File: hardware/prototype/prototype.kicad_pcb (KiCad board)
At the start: 2 copper layers, 177.8 x 111.8 mm, 91 parts, among them J1 0734120114, J2 Conn_01x04, J4 Conn_01x04, J5 Conn_02x07_Odd_Even, J6 Battery-holder, J7 Conn_02x12_Odd_Even, J8 Jack-DC, Q1 DTC143Z, Q2 Si2323, U1 QUECTEL_L80, U2 TLV71333PDBV, U3 LM2596_MODULE, U4 DevkitC, U5 MIKROE_3G_CLICK

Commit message: Complete PCB layout
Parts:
- removed D10, D13, D14, D15, D16, D17, D18, D7, D8, D9: D_TVS, Diode_SMD:D_0402_1005Metric
- removed D11, D12: D_TVS, digikey-footprints:DO-214AC
- removed D19, D20: LED, LED_SMD:LED_0805_2012Metric_Pad0.97x1.50mm_HandSolder
- removed J8: Jack-DC, Connector_BarrelJack:BarrelJack_Horizontal
- removed TP1: Test_Point_Probe, TestPoint:TestPoint_Pad_D1.0mm
- added G***: LOGO, logo:LoRa_logo, F.Cu at (115.6, 124.5)
- added J3: Conn_01x04, lib_fp:PinHeader_1x04_P2.54mm_staggered_Vertical, F.Cu at (182.4, 110.2)
- C10, C16: value 220uF -> 0.1uF; footprint Capacitor_SMD:CP_Elec_6.3x5.8 -> Capacitor_SMD:C_0805_2012Metric_Pad1.15x1.50mm_HandSolder
- C12, C15: value 0.1uF -> 220uF; footprint Capacitor_SMD:C_0805_2012Metric_Pad1.15x1.50mm_HandSolder -> Capacitor_SMD:CP_Elec_6.3x5.8
- C2: value 0.1uF -> 10uF
- C3: value 10uF -> 1uF
- C4: value 1uF -> 0.1uF
- D1, D2: value LED -> D_TVS; footprint LED_SMD:LED_0805_2012Metric_Pad0.97x1.50mm_HandSolder -> digikey-footprints:DO-214AC
- D3, D4, D5, D6: value D_TVS -> LED; footprint Diode_SMD:D_0402_1005Metric -> LED_SMD:LED_0805_2012Metric_Pad0.97x1.50mm_HandSolder
- J1: value 0734120114 -> Jack-DC; footprint digikey-footprints:Molex_734120114_UMC_RF_CONN_Vertical -> Connector_BarrelJack:BarrelJack_Horizontal
- J2: value Conn_01x04 -> 0734120114; footprint lib_fp:PinHeader_1x04_P2.54mm_staggered_Vertical -> digikey-footprints:Molex_734120114_UMC_RF_CONN_Vertical
- JP17: value Jumper -> Jumper_NC_Dual; footprint lib_fp:PinHeader_1x02_P2.54mm_staggered_Vertical -> lib_fp:PinHeader_1x03_P2.54mm_staggered_Vertical
- JP19: value SolderJumper_2_Open -> Jumper; footprint Jumper:SolderJumper-2_P1.3mm_Open_RoundedPad1.0x1.5mm -> lib_fp:PinHeader_1x02_P2.54mm_staggered_Vertical
- JP21: value Jumper -> SolderJumper_2_Open; footprint lib_fp:PinHeader_1x02_P2.54mm_staggered_Vertical -> Jumper:SolderJumper-2_P1.3mm_Open_RoundedPad1.0x1.5mm
- Q1: value DTC143Z -> Si2323; footprint Package_TO_SOT_SMD:SC-59_Handsoldering -> Package_TO_SOT_SMD:SOT-23
- Q2: value Si2323 -> DTC143Z; footprint Package_TO_SOT_SMD:SOT-23 -> Package_TO_SOT_SMD:SC-59_Handsoldering
- R2: value 110R -> 10k
- R5: value 10k -> 4.7k
- R6: value 130R -> 33R
- R7: value 4.7k -> 1.5k
- R8: value 33R -> 110R
- R9: value 1.5k -> 130R
- moved C1 382.9 mm to (90.2, 84.6), turned to 90 degrees
- moved GDT1 376.3 mm to (85.1, 45.0), turned to 270 degrees
- moved JP6 373.4 mm to (99.1, 74.3)
- moved F1 370.4 mm to (91.7, 45.0)
- moved U2 364.5 mm to (107.7, 86.1)
- moved C2 363.6 mm to (92.7, 84.6), turned to 90 degrees
- moved JP18 362.0 mm to (119.4, 70.2), turned to 270 degrees
- moved C6 359.5 mm to (124.7, 69.0), turned to 90 degrees
- moved JP1 356.4 mm to (105.2, 108.2), turned to 180 degrees
- moved R4 355.2 mm to (129.2, 70.5)
- moved C3 353.1 mm to (104.4, 83.8), turned to 90 degrees
- moved R7 351.5 mm to (133.5, 102.7)
- moved J1 343.0 mm to (104.1, 38.2), turned to 270 degrees
- moved C4 334.2 mm to (85.7, 85.2)
- moved C13 332.8 mm to (160.1, 129.3), turned to 90 degrees
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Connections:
- C1 pad 1: GND -> /GLOBAL_3V3
- C1 pad 2: /BRD_GPS_VBCKUP -> GND
- C3 pad 1: /GLOBAL_3V3 -> /CELLULAR_5V
- C4 pad 1: /CELLULAR_5V -> GND
- C4 pad 2: GND -> /BRD_GPS_VBCKUP
- D1 pad 2: /GLOBAL_3V3 -> GND
- D2 pad 2: /NETWORK_STATUS -> GND
- D3 pad 1: /RMII_TX1 -> Net-(D3-Pad1)
- D3 pad 2: GND -> /GLOBAL_3V3
- D4 pad 1: /RMII_CRS_DV -> Net-(D4-Pad1)
- D4 pad 2: GND -> /NETWORK_STATUS
- D5 pad 1: /RMII_TX0 -> Net-(D5-Pad1)
- D5 pad 2: GND -> /GLOBAL_3V3
- D6 pad 1: /RMII_MDIO -> Net-(D6-Pad1)
- D6 pad 2: GND -> /CELLULAR_5V
- F1 pad 1: /(+)RAIL -> /12v_rail
- F1 pad 2: Net-(D11-Pad1) -> Net-(D1-Pad1)
- F2 pad 1: Net-(F2-Pad1) -> /5v_rail
- F2 pad 2: Net-(D12-Pad1) -> Net-(D2-Pad1)
- GDT1 pad 1: /(+)RAIL -> /12v_rail
- GDT2 pad 1: Net-(F2-Pad1) -> /5v_rail
- J1 pad 1: GND -> /Power_Input
- J1 pad 2: Net-(J1-Pad2) -> GND
- J2 pad 1: /GLOBAL_3V3 -> GND
- J2 pad 2: /TEMP_DATA -> Net-(J2-Pad2)
- JP11 pad 1: /V_BCKUP -> /12v_rail
- JP11 pad 2: /BRD_GPS_VBCKUP -> /Power_Input
- JP11 pad 3: /GLOBAL_3V3 -> /5v_rail
- JP16 pad 1: Net-(JP16-Pad1) -> /V_BCKUP
- JP16 pad 2: /23 -> /BRD_GPS_VBCKUP
- JP16 pad 3: GND -> /GLOBAL_3V3
- JP17 pad 1: /CELLULAR_5V -> Net-(JP17-Pad1)
- JP17 pad 2: /ESP32_5v -> /23
- JP18 pad 1: Net-(JP18-Pad1) -> /CELLULAR_5V
- JP18 pad 2: Net-(F2-Pad1) -> /ESP32_5v
- JP19 pad 1: Net-(J6-Pad1) -> Net-(JP19-Pad1)
- JP19 pad 2: /V_BCKUP -> /5v_rail
- JP20 pad 1: /(+)RAIL -> Net-(D2-Pad1)
- JP20 pad 2: Net-(F2-Pad1) -> /CELLULAR_5V
- JP21 pad 1: /CELLULAR_5V -> Net-(J6-Pad1)
- JP21 pad 2: Net-(D12-Pad1) -> /V_BCKUP
- JP6 pad 1: Net-(J1-Pad2) -> Net-(J2-Pad2)
- Q1 pad 1: /PPS_VISUAL -> GND
- Q1 pad 2: GND -> /V_BCKUP
- Q1 pad 3: Net-(Q1-Pad3) -> Net-(J6-Pad1)
- Q2 pad 1: GND -> /PPS_VISUAL
- Q2 pad 2: /V_BCKUP -> GND
- Q2 pad 3: Net-(J6-Pad1) -> Net-(Q2-Pad3)
- R10 pad 2: Net-(D19-Pad1) -> Net-(D5-Pad1)
- R11 pad 2: Net-(D20-Pad1) -> Net-(D6-Pad1)
- R2 pad 1: Net-(Q1-Pad3) -> /STATUS
- R2 pad 2: Net-(D1-Pad1) -> GND
- R5 pad 1: /STATUS -> /GLOBAL_3V3
- R5 pad 2: GND -> /RMII_REFOSC_nINT
- R6 pad 1: GND -> /RMII_REFOSC_nINT
- R6 pad 2: Net-(D2-Pad1) -> Net-(J5-Pad7)
- R7 pad 2: /RMII_REFOSC_nINT -> /RMII_MDIO
- R8 pad 1: /RMII_REFOSC_nINT -> Net-(Q2-Pad3)
- R8 pad 2: Net-(J5-Pad7) -> Net-(D3-Pad1)
- R9 pad 1: /GLOBAL_3V3 -> GND
- R9 pad 2: /RMII_MDIO -> Net-(D4-Pad1)
- U3 pad 1: Net-(D11-Pad1) -> Net-(D1-Pad1)
- U3 pad 3: Net-(JP18-Pad1) -> Net-(JP19-Pad1)
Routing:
- net Net-(J2-Pad2): track 0.00 -> 163.9 mm, vias 0 -> 2
- net /SCK: track 0.00 -> 153.5 mm, vias 0 -> 5
- net /CSN: track 0.00 -> 137.8 mm, vias 0 -> 11
- net /GLOBAL_3V3: track 0.00 -> 132.1 mm, vias 0 -> 9
- net /RESET: track 0.00 -> 130.2 mm, vias 0 -> 7
- net /16: track 0.00 -> 120.0 mm
- net /22: track 0.00 -> 120.0 mm
- net /15: track 0.00 -> 120.0 mm
- net /20: track 0.00 -> 120.0 mm
- net /14: track 0.00 -> 120.0 mm, vias 0 -> 1
- net /17: track 0.00 -> 120.0 mm
- net /19: track 0.00 -> 120.0 mm
- net /21: track 0.00 -> 120.0 mm
- net /23: track 0.00 -> 120.0 mm
- net /ESP32_5v: track 0.00 -> 115.8 mm, vias 0 -> 5
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- added copper zone on B.Cu, net /CELLULAR_5V
- added copper zone on F.Cu, net /CELLULAR_5V
- added copper zone on F.Cu, net /GLOBAL_3V3
- added copper zone on B.Cu, net GND
- added copper zone on F.Cu, net GND
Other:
- outline, holes or cut-outs redrawn
- net class 1A_class added: clearance 0.2, trace_width 0.301498, via_dia 0.8, via_drill 0.4
- net class 3A_class added: clearance 0.2, trace_width 1.3462, via_dia 0.8, via_drill 0.4
- board text added: "3V3_OK"
- board text added: "5V"
- board text added: "5V_OK"
- board text added: "Backup_disable"
- board text added: "CR2032_Backup"
- board text added: "GPS_OK"
- board text added: "LAN_module"
- board text added: "LoRa_concentrator"
- board text added: "MIKROE_Cellular_module"
- board text added: "NET_STAT"
- board text added: "Other"
- board text added: "PPS_LED"
- board text added: "PPS_uFl"
- board text added: "RAK831"
- board text added: "RHFM0301"
- board text added: "[RHFM||RAK]"

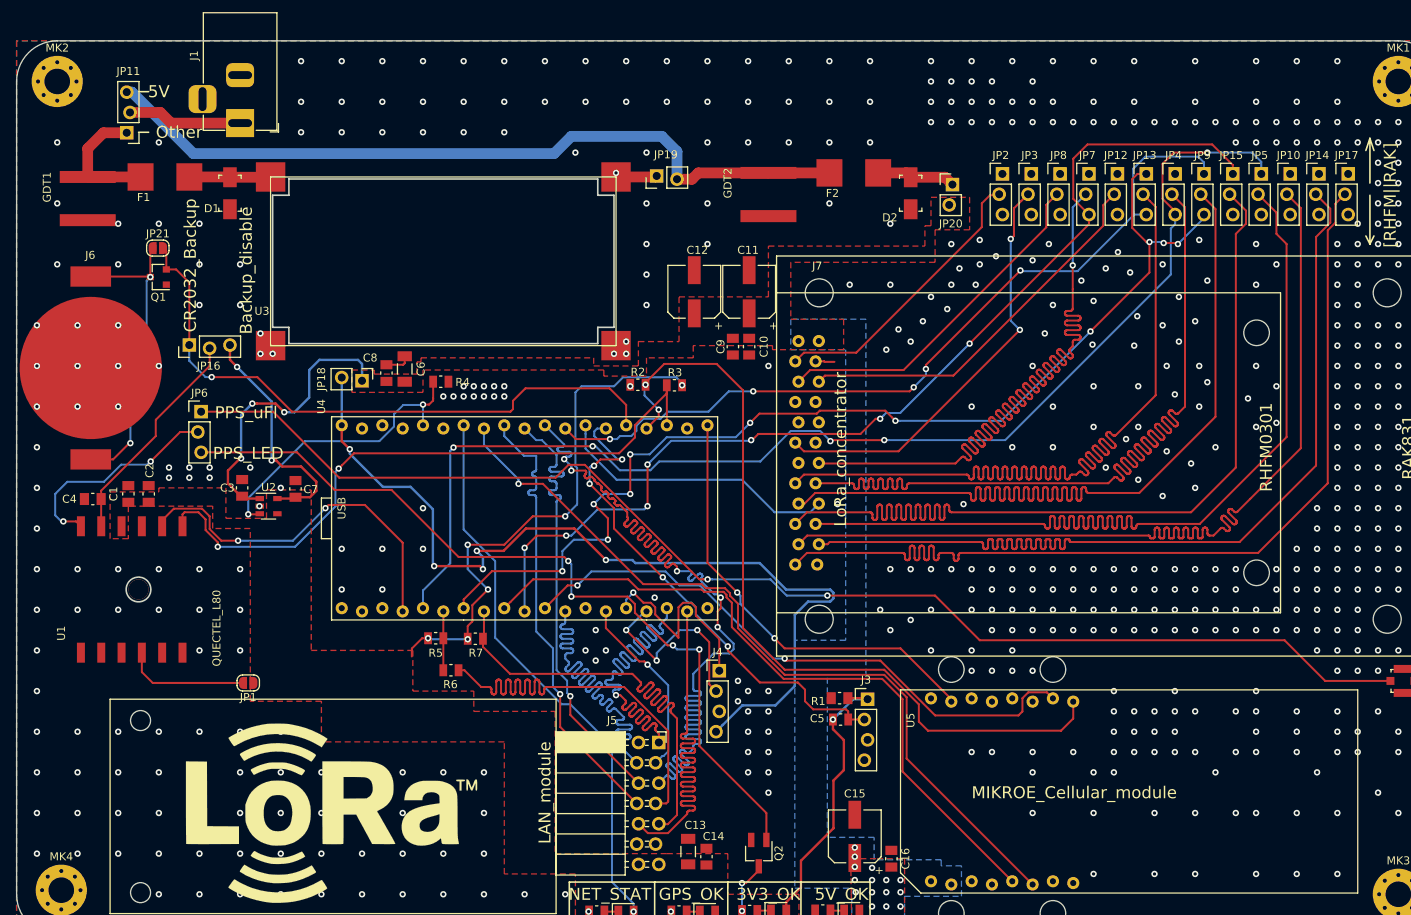
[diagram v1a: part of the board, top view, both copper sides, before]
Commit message: Modify PCB layout
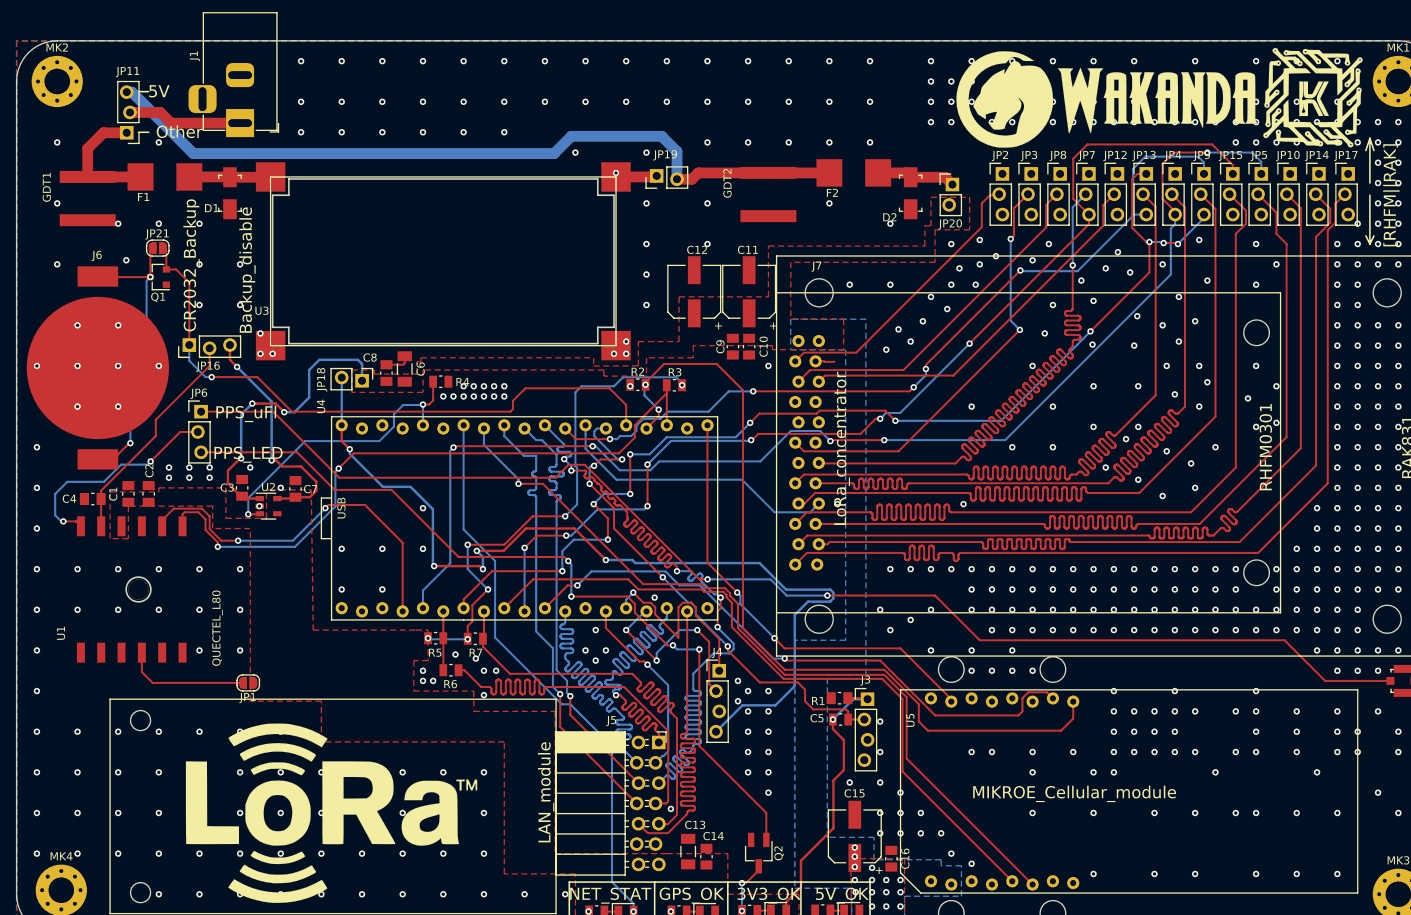
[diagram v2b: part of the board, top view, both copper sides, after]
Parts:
- added G***: LOGO, logo:Wakanda_logo, F.Cu at (212.5, 35.3)
- added G***: LOGO, logo:Kaiote_logo, F.Cu at (238.3, 35.1)
- moved J6 0.89 mm to (86.4, 68.8)
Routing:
- net /GLOBAL_3V3: track 132.1 -> 128.5 mm
- net Net-(J6-Pad1): track 38.8 -> 38.0 mm
- net GND: vias 591 -> 612

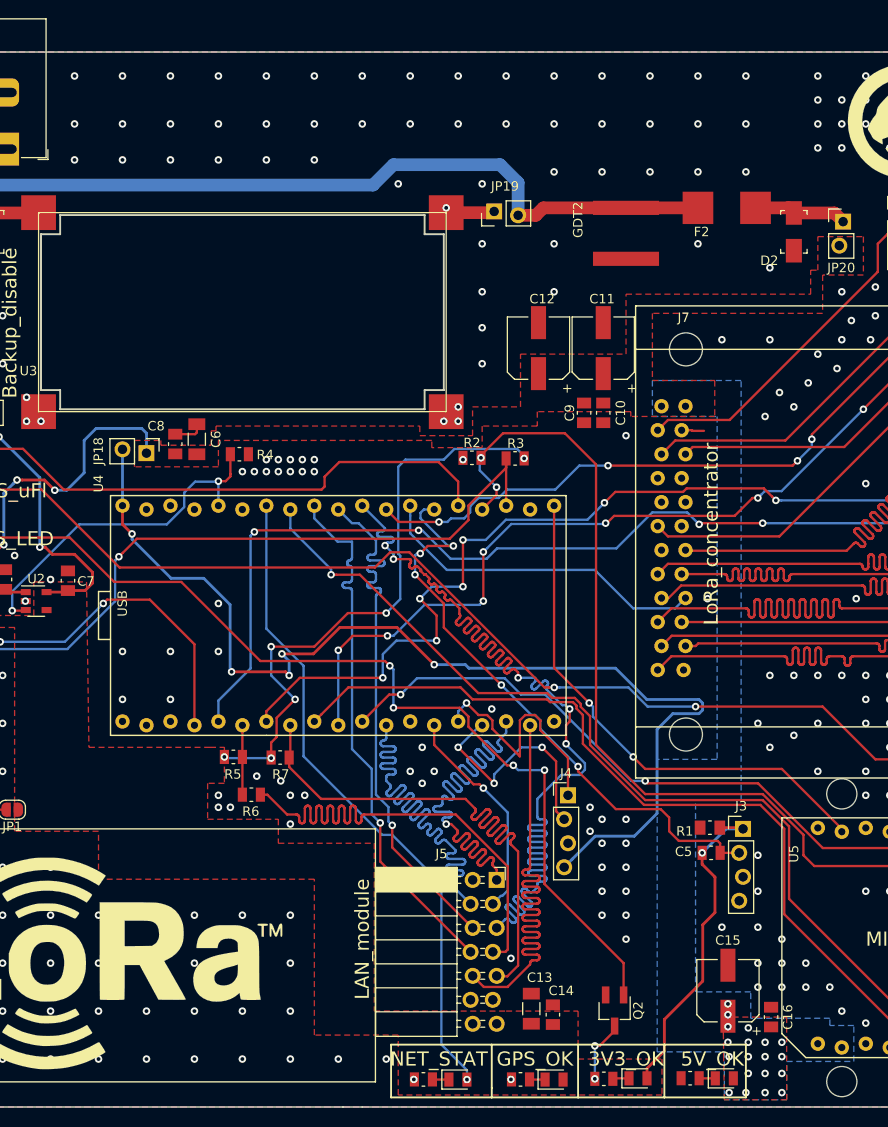
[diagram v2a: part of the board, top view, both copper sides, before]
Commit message: Complete PCB design, BOM generation and gerber generation
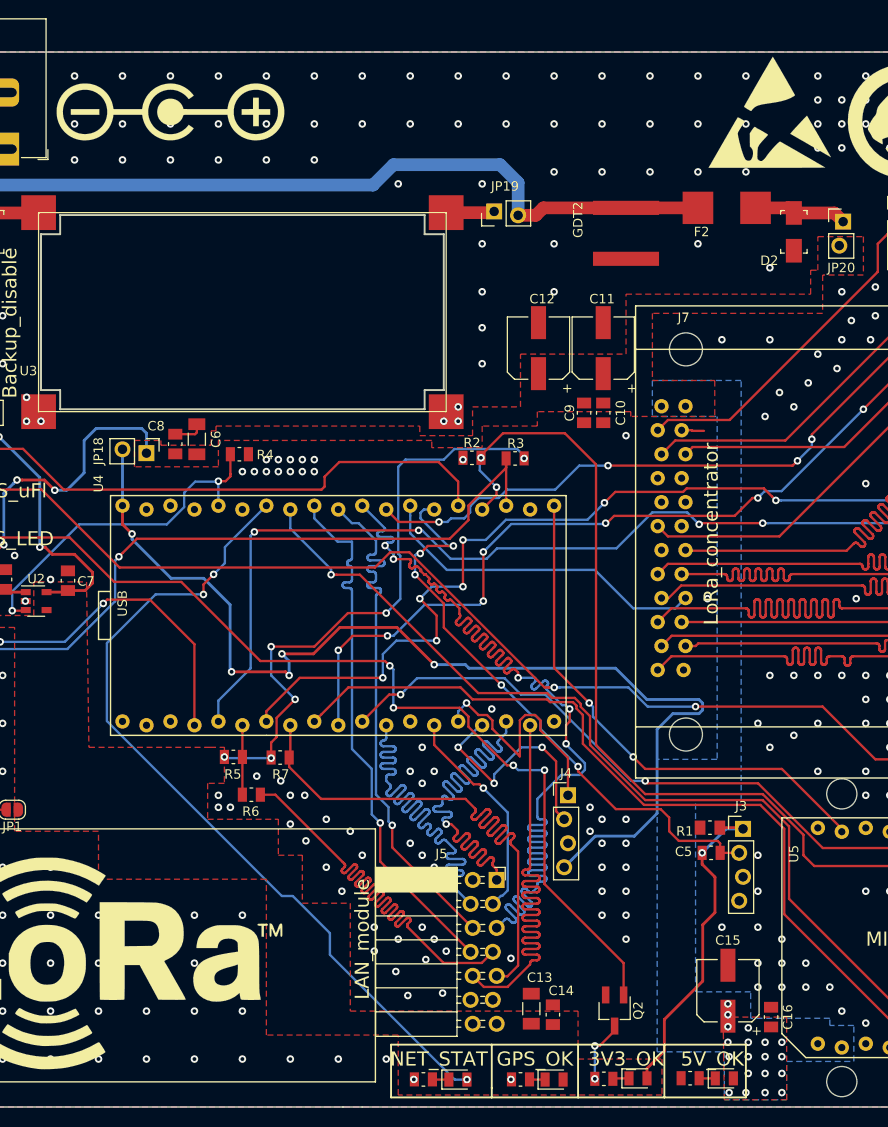
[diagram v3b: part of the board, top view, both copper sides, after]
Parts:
- added REF**: Polarity_Center_Positive_6mm_SilkScreen, Symbol:Polarity_Center_Positive_6mm_SilkScreen, F.Cu at (121.9, 34.3)
- added REF**: ESD-Logo_13.2x12mm_SilkScreen, Symbol:ESD-Logo_13.2x12mm_SilkScreen, F.Cu at (185.4, 34.3)
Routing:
- net /NETWORK_STATUS: track 70.2 -> 88.0 mm, vias 1 -> 3
- net Net-(JP19-Pad1): vias 1 -> 0
- net GND: vias 612 -> 622
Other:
- net class 33_ohm_microstrip added: clearance 0.2, trace_width 0.25, via_dia 0.8, via_drill 0.4
